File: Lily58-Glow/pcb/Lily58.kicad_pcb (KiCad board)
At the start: 2 copper layers, 142.5 x 106.3 mm, 124 parts, among them J1 LED, J2 4PIN, J3 , P1 i2c_pin, P2 i2c_pin, P3 ICSP, P4 OLED, P5 i2c_pin, P6 i2c_pin, SW1 SW_PUSH, SW10 SW_PUSH, SW11 SW_PUSH, SW12 SW_PUSH, SW13 SW_PUSH, SW14 SW_PUSH, SW15 SW_PUSH, SW16 SW_PUSH, SW17 SW_PUSH, SW18 SW_PUSH, SW19 SW_PUSH, SW2 SW_PUSH, SW20 SW_PUSH, SW21 SW_PUSH, SW22 SW_PUSH, SW23 SW_PUSH, SW24 SW_PUSH, SW25 SW_PUSH, SW26 SW_PUSH, SW27 SW_PUSH, SW28 SW_PUSH, SW29 SW_PUSH, SW3 SW_PUSH, SW30 , SW31 , SW32 , SW4 SW_PUSH, SW5 SW_PUSH, SW6 SW_PUSH, SW7 SW_PUSH, SW8 SW_PUSH, SW9 SW_PUSH, U1 ProMicro

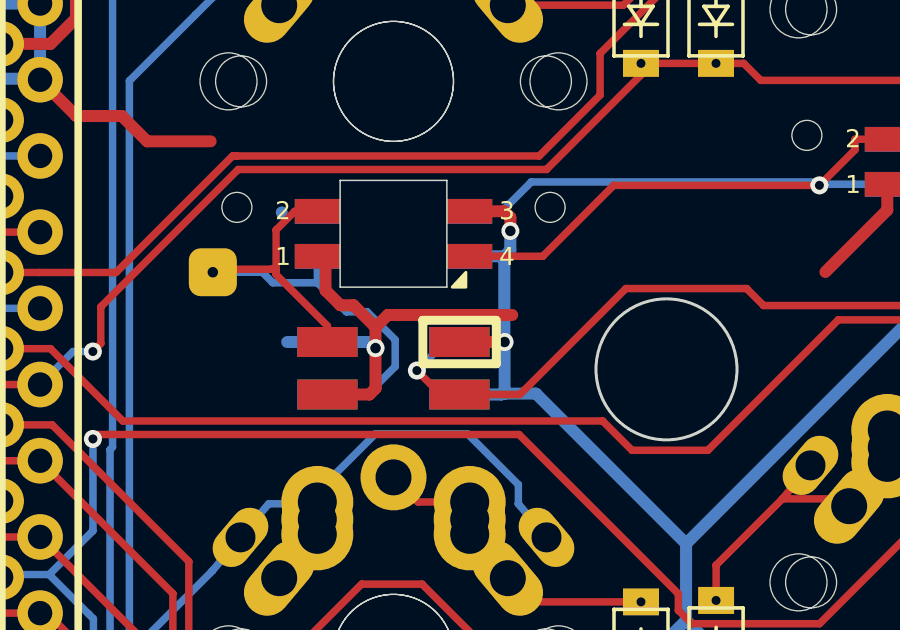
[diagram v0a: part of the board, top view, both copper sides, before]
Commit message: add some keyboard
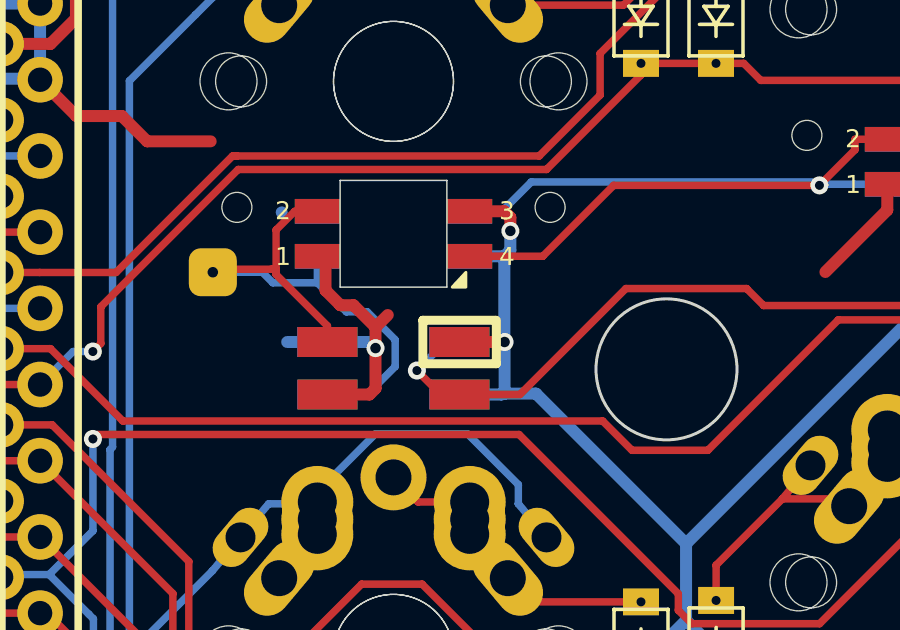
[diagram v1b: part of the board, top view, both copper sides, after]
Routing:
- net GND: track 288.6 -> 284.5 mm
